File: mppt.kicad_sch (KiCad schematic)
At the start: 48 parts, among them J10 Fan_F, J9 Fan_M, M1 Fan_3pin, Q1 IPP019N08NF2S, Q2 IPP019N08NF2S, Q3 IPP019N08NF2S, Q4 Si2306BDS, Q5 Si2306BDS, U3 ACS758xCB, U4 L6398D, U5 TME 1212S, U6 ACS758xCB

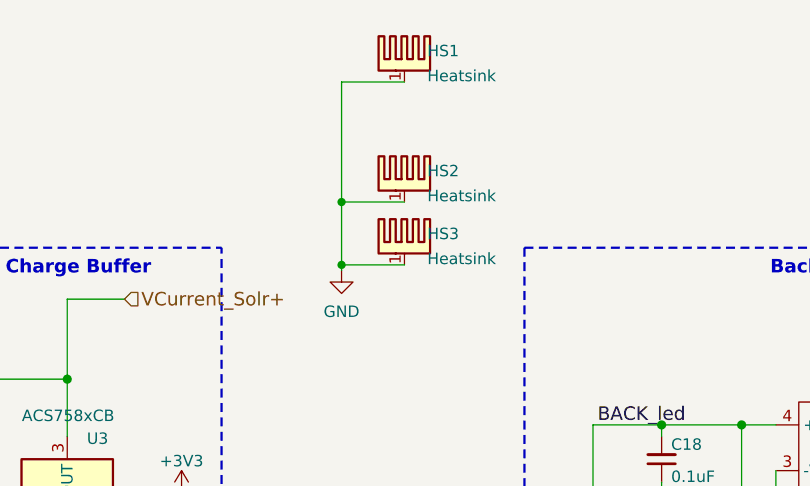
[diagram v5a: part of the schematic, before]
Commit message: Fix some errors in the design (esp net-tie in wrong place)
 - correct led, diode footprints & model
 - fix fuse holder (bad hole spec)
 - update oled mod
 - update EC11 mod
 - add Blender models of case (xz compressed)
 - more updated gerbers (not current!)
 - improve layout of front panel pcb
 - delete unused files
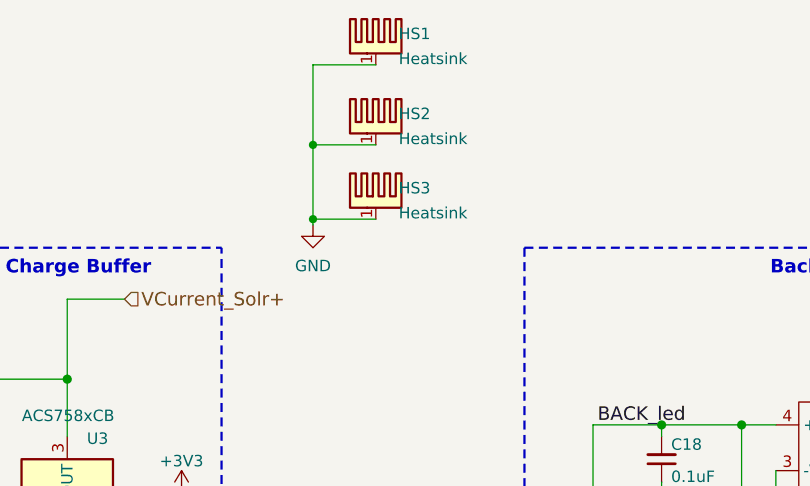
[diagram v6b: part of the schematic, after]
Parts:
- C20: footprint Capacitor_SMD:C_1210_3225Metric_Pad1.33x2.70mm_HandSolder -> Capacitor_SMD:C_0805_2012Metric_Pad1.18x1.45mm_HandSolder
- CP1: Part UPM1H221MHD6TD -> UPM1H221MHD6TO; Vendor Cost 0.587 -> 0.653; Vendor SKU 647-UPM1H221MHD6TD -> 647-UPM1H221MHD6TO
- HS1, HS2, HS3: footprint MountingHole:MountingHole_2.2mm_M2_Pad_Via -> MountingHole:MountingHole_2.7mm_M2.5_Pad_Via
- Q1, Q2, Q3: Vendor SKU 942-IPP019N08NF2S -> 726-IPP019N08NF2SAKM
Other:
- moved on the sheet: HS1, HS2, HS3

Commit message: Adjust to supply 2 CS sigs to display; rename MISO to DC; larger conn cable.
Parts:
- J10, M1: footprint ~ -> (none)
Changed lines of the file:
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@@
   (title_block
     (title "SolarPump v3")
-    (date "2022-03-09")
+    (date "2022-05-18")
     (rev "1.1")
     (company "IvimeyCom")
@@
     (property "Reference" "J10" (id 0) (at 250.2154 37.8756 0))
     (property "Value" "Fan_F" (id 1) (at 253.5174 46.6285 0))
-    (property "Footprint" "~" (id 2) (at 249.555 41.91 0)
+    (property "Footprint" "" (id 2) (at 249.555 41.91 0)
       (effects (font (size 1.27 1.27)) hide)
     )
@@
       (effects (font (size 1.27 1.27)) (justify left))
     )
-    (property "Footprint" "~" (id 2) (at 267.335 42.926 0)
-      (effects (font (size 1.27 1.27)) hide)
-    )
+    (property "Footprint" "" (id 2) (at 267.335 42.926 0)
+      (effects (font (size 1.27 1.27)) hide)
+    )

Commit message: Lots of small changes; widen disp board to same as pwr board; use attiny mcu for rot-enc ctrl; switch to one board with cutline
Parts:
- F1, F2: footprint Fuse:Fuseholder_Keystone_3555-2 -> Fuse:Fuseholder_Cylinder-5x20mm_Schurter_0031_8201_Horizontal_Open
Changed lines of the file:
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@@
       (effects (font (size 1.27 1.27)) (justify right))
     )
-    (property "Footprint" "Fuse:Fuseholder_Keystone_3555-2" (id 2) (at 25.908 94.615 90)
+    (property "Footprint" "Fuse:Fuseholder_Cylinder-5x20mm_Schurter_0031_8201_Horizontal_Open" (id 2) (at 25.908 94.615 90)
       (effects (font (size 1.27 1.27)) hide)
     )
@@
     (property "Reference" "F2" (id 0) (at 247.65 127.9864 90))
     (property "Value" "Fuse 25A" (id 1) (at 247.65 130.7615 90))
-    (property "Footprint" "Fuse:Fuseholder_Keystone_3555-2" (id 2) (at 247.65 134.493 90)
+    (property "Footprint" "Fuse:Fuseholder_Cylinder-5x20mm_Schurter_0031_8201_Horizontal_Open" (id 2) (at 247.65 134.493 90)
       (effects (font (size 1.27 1.27)) hide)
     )
@@
     )
     (property "Vendor Cost" "~" (id 6) (at 92.075 34.925 0)
+      (effects (font (size 1.27 1.27)) hide)
+    )
+    (property "Vendor" "~" (id 7) (at 92.075 34.925 0)
+      (effects (font (size 1.27 1.27)) hide)
+    )
+    (property "Vendor SKU" "~" (id 8) (at 92.075 34.925 0)
       (effects (font (size 1.27 1.27)) hide)
     )
@@
       (effects (font (size 1.27 1.27)) hide)
     )
+    (property "Vendor" "~" (id 7) (at 92.075 17.78 0)
+      (effects (font (size 1.27 1.27)) hide)
+    )
+    (property "Vendor SKU" "~" (id 8) (at 92.075 17.78 0)
+      (effects (font (size 1.27 1.27)) hide)
+    )
     (pin "1")
   )
@@
       (effects (font (size 1.27 1.27)) hide)
     )
+    (property "Vendor" "~" (id 7) (at 92.075 26.67 0)
+      (effects (font (size 1.27 1.27)) hide)
+    )
+    (property "Vendor SKU" "~" (id 8) (at 92.075 26.67 0)
+      (effects (font (size 1.27 1.27)) hide)
+    )
